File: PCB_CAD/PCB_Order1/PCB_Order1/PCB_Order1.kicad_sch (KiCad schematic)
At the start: 10 parts, among them IC1 TC58BVG1S3HTA00, J1 FW6190, U1 STM32H7A3ZITx, U2 AK5720VT

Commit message: made some small changes to kicad schematic to print
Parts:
- added IC2: AS4C8M16SA-6TCN, SOP80P1176X120-54N, symbol AS4C8M16SA-6TCN:AS4C8M16SA-6TCN
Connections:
- net RAM_A0: now reaches U1.10 (PF0)
- net RAM_A0: now also IC2.23 (A0)
- net RAM_A1: now reaches U1.11 (PF1)
- net RAM_A1: now also IC2.24 (A1)
- net RAM_A2: now reaches U1.12 (PF2)
- net RAM_A2: now also IC2.25 (A2)
- net RAM_A3: now reaches U1.13 (PF3)
- net RAM_A3: now also IC2.26 (A3)
- net RAM_A4: now reaches U1.14 (PF4)
- net RAM_A4: now also IC2.29 (A4)
- net RAM_A5: now reaches U1.15 (PF5)
- net RAM_A5: now also IC2.30 (A5)
- net RAM_A6: now reaches U1.50 (PF12)
- net RAM_A6: now also IC2.31 (A6)
- net RAM_A7: now reaches U1.53 (PF13)
- net RAM_A7: now also IC2.32 (A7)
- net RAM_A8: now reaches U1.54 (PF14)
- net RAM_A8: now also IC2.33 (A8)
- net RAM_A9: now reaches U1.55 (PF15)
- net RAM_A9: now also IC2.34 (A9)
- net RAM_A10: now reaches U1.56 (PG0)
- net RAM_A10: now also IC2.22 (A10/AP)
- net RAM_A11: now reaches U1.57 (PG1)
- net RAM_A11: now also IC2.35 (A11)
- net RAM_BA0: now reaches U1.89 (PG4)
- net RAM_BA0: now also IC2.20 (BA0)
- net RAM_BA1: now reaches U1.90 (PG5)
- net RAM_BA1: now also IC2.21 (BA1)
- new net RAM_ChipEnable: IC2.19 (CS#)
- new net RAM_Clock: IC2.38 (CLK)
- new net RAM_ClockEnable: IC2.37 (CKE)
- new net RAM_ColumnStrobe: IC2.17 (CAS#)
- new net RAM_DQ0: IC2.2 (DQ0)
- new net RAM_DQ1: IC2.4 (DQ1)
- new net RAM_DQ10: IC2.45 (DQ10)
- new net RAM_DQ11: IC2.47 (DQ11)
- new net RAM_DQ12: IC2.48 (DQ12)
- new net RAM_DQ13: IC2.50 (DQ13)
- new net RAM_DQ14: IC2.51 (DQ14)
- new net RAM_DQ15: IC2.53 (DQ15)
- new net RAM_DQ2: IC2.5 (DQ2)
- new net RAM_DQ3: IC2.7 (DQ3)
- new net RAM_DQ4: IC2.8 (DQ4)
- new net RAM_DQ5: IC2.10 (DQ5)
- new net RAM_DQ6: IC2.11 (DQ6)
- new net RAM_DQ7: IC2.13 (DQ7)
- new net RAM_DQ8: IC2.42 (DQ8)
- new net RAM_DQ9: IC2.44 (DQ9)
- new net RAM_LDQM: IC2.15 (LDQM)
- new net RAM_RowStrobe: IC2.18 (RAS#)
- new net RAM_UDQM: IC2.39 (UDQM)
- new net RAM_WriteEnable: IC2.16 (WE#)
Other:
- moved on the sheet: C1, C2, C3, C4, C5, C6, IC1, J1, U1, U2

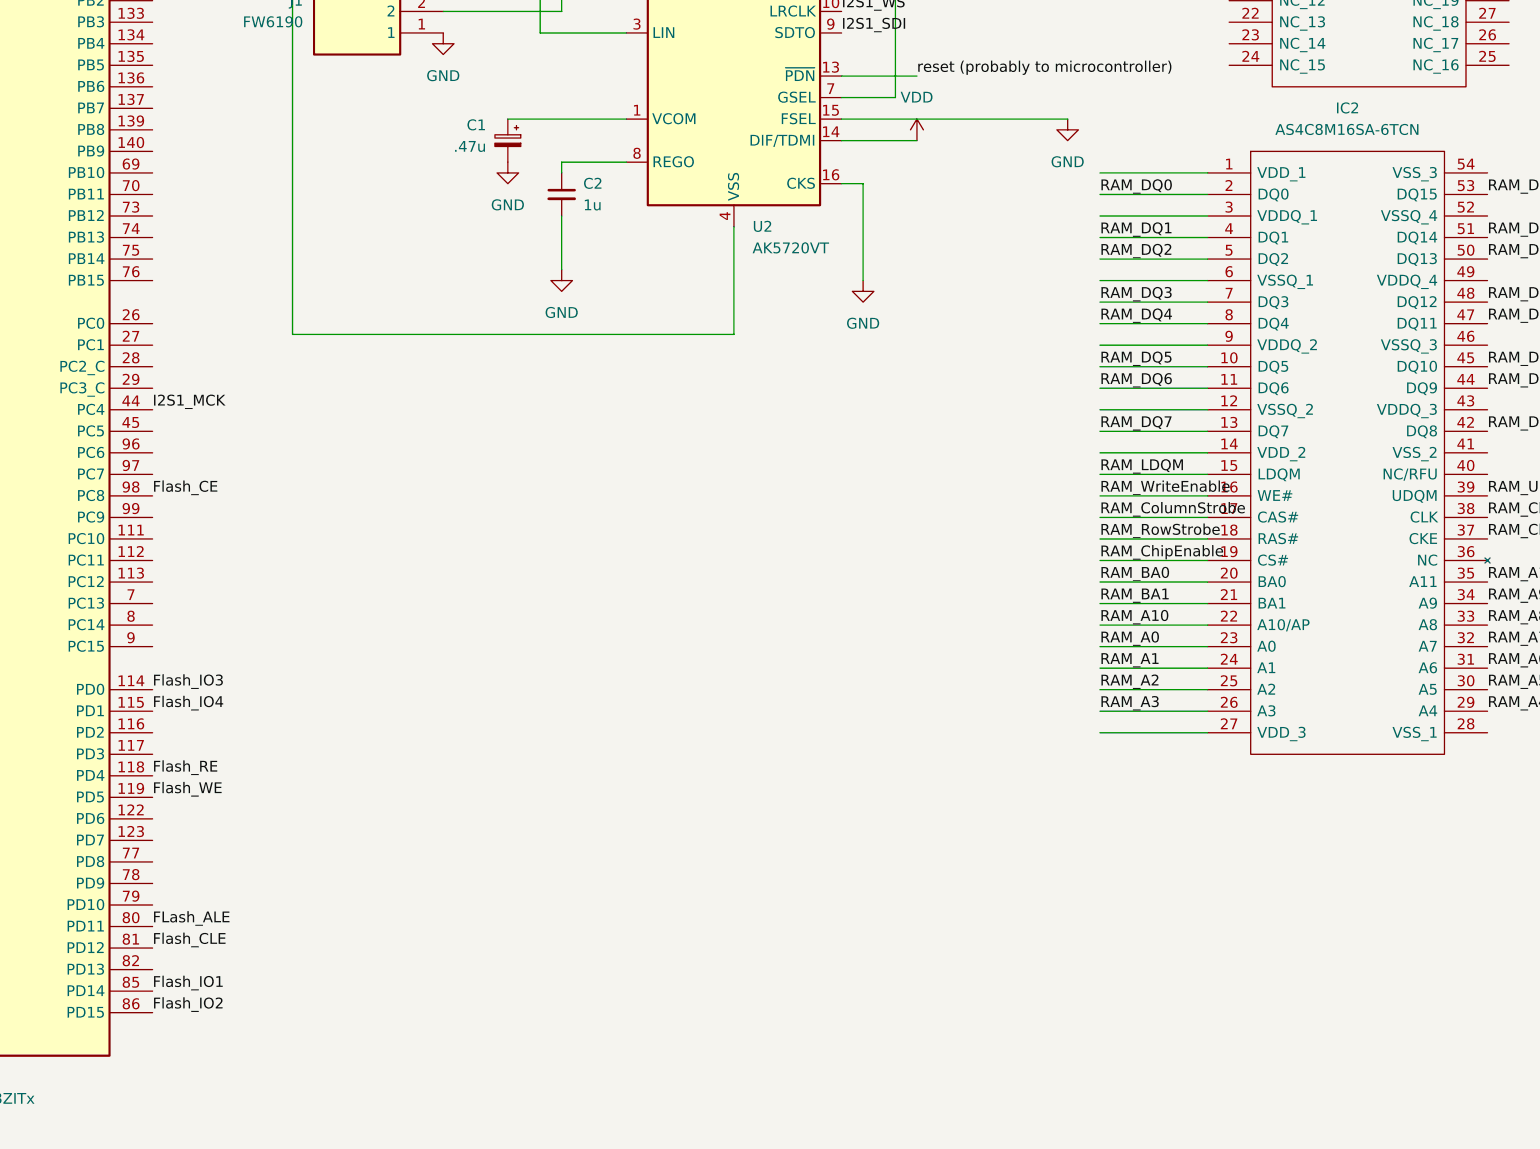
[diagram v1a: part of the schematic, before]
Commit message: schematic add NAU8402WG DAC
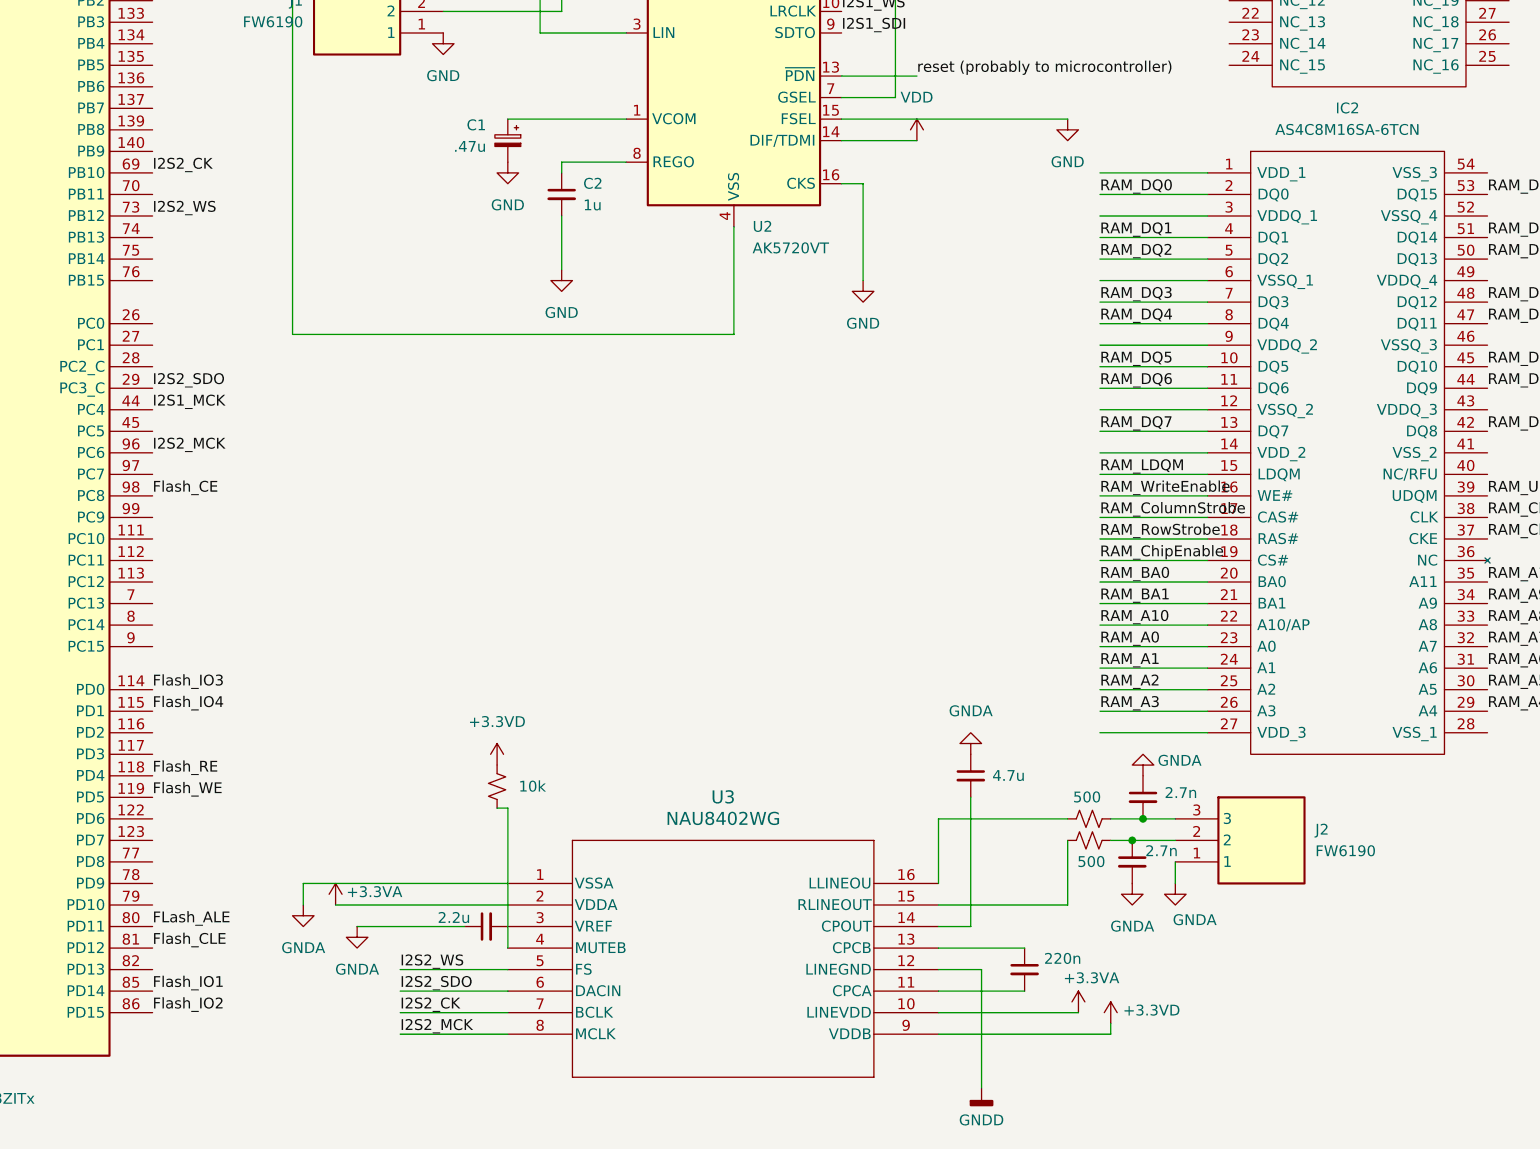
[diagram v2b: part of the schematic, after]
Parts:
- added CPC: 220n, symbol Device:C_Small
- added Chargepump_out: 4.7u, symbol Device:C_Small
- added DacLout_cap, DacRout_cap: 2.7n, symbol Device:C_Small
- added DacLout_res, DacRout_res: 500, symbol Device:R_Small_US
- added Dac_vref: 2.2u, symbol Device:C_Small
- added J2: FW6190, FW6190, symbol FW6190:FW6190
- added Mute_tie: 10k, symbol Device:R_Small_US
- added U3: NAU8402WG, TSSOP16_NAU8402_NUV, symbol NAU8402WG:NAU8402WG
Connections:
- net I2S2_SDO: now reaches U1.29 (PC3_C)
- net I2S2_SDO: now also U3.6 (DACIN)
- net I2S2_CK: now reaches U1.69 (PB10)
- net I2S2_CK: now also U3.7 (BCLK)
- net I2S2_WS: now reaches U1.73 (PB12)
- net I2S2_WS: now also U3.5 (FS)
- net I2S2_MCK: now reaches U1.96 (PC6)
- net I2S2_MCK: now also U3.8 (MCLK)
- new net: DacLout_res.1, U3.16 (LLINEOU)
- new net: DacLout_cap.2, DacLout_res.2, J2.3
- new net: CPC.1, U3.13 (CPCB)
- new net: CPC.2, U3.11 (CPCA)
- new net: DacRout_res.1, U3.15 (RLINEOUT)
- new net: DacRout_cap.1, DacRout_res.2, J2.2
- new net: Chargepump_out.2, U3.14 (CPOUT)
- new net: Dac_vref.2, U3.3 (VREF)
- new net: Mute_tie.2, U3.4 (MUTEB)
- new net +3.3VA: U3.10 (LINEVDD), U3.2 (VDDA)
- new net +3.3VD: Mute_tie.1, U3.9 (VDDB)
- new net GNDA: Chargepump_out.1, DacLout_cap.1, DacRout_cap.2, Dac_vref.1, J2.1, U3.1 (VSSA)
- new net GNDD: U3.12 (LINEGND)

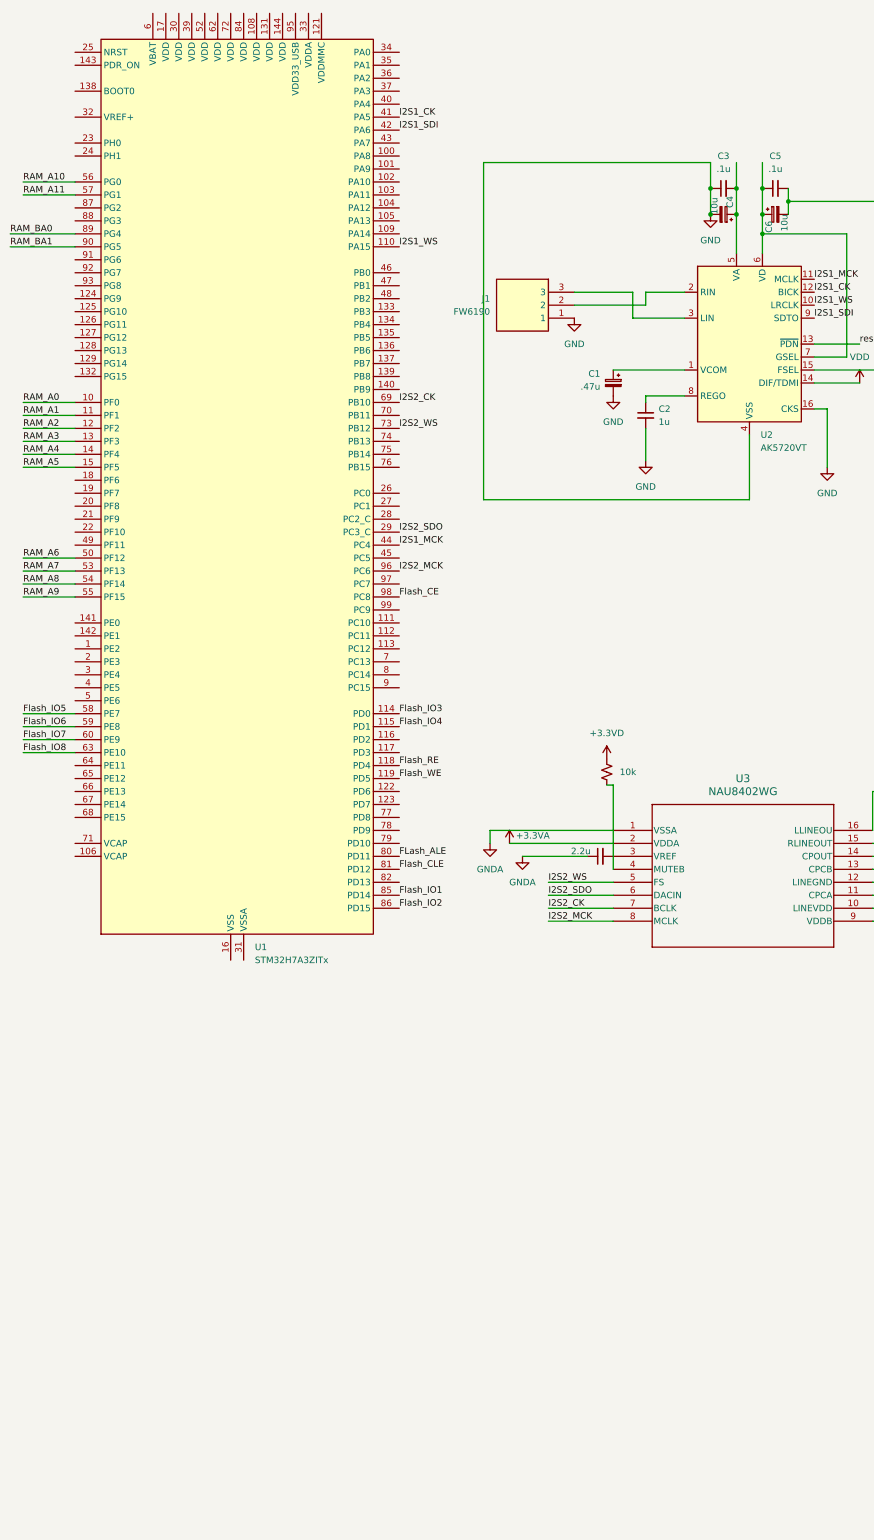
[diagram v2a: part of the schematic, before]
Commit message: add spdif tx output, fixed DIX9211 cad model
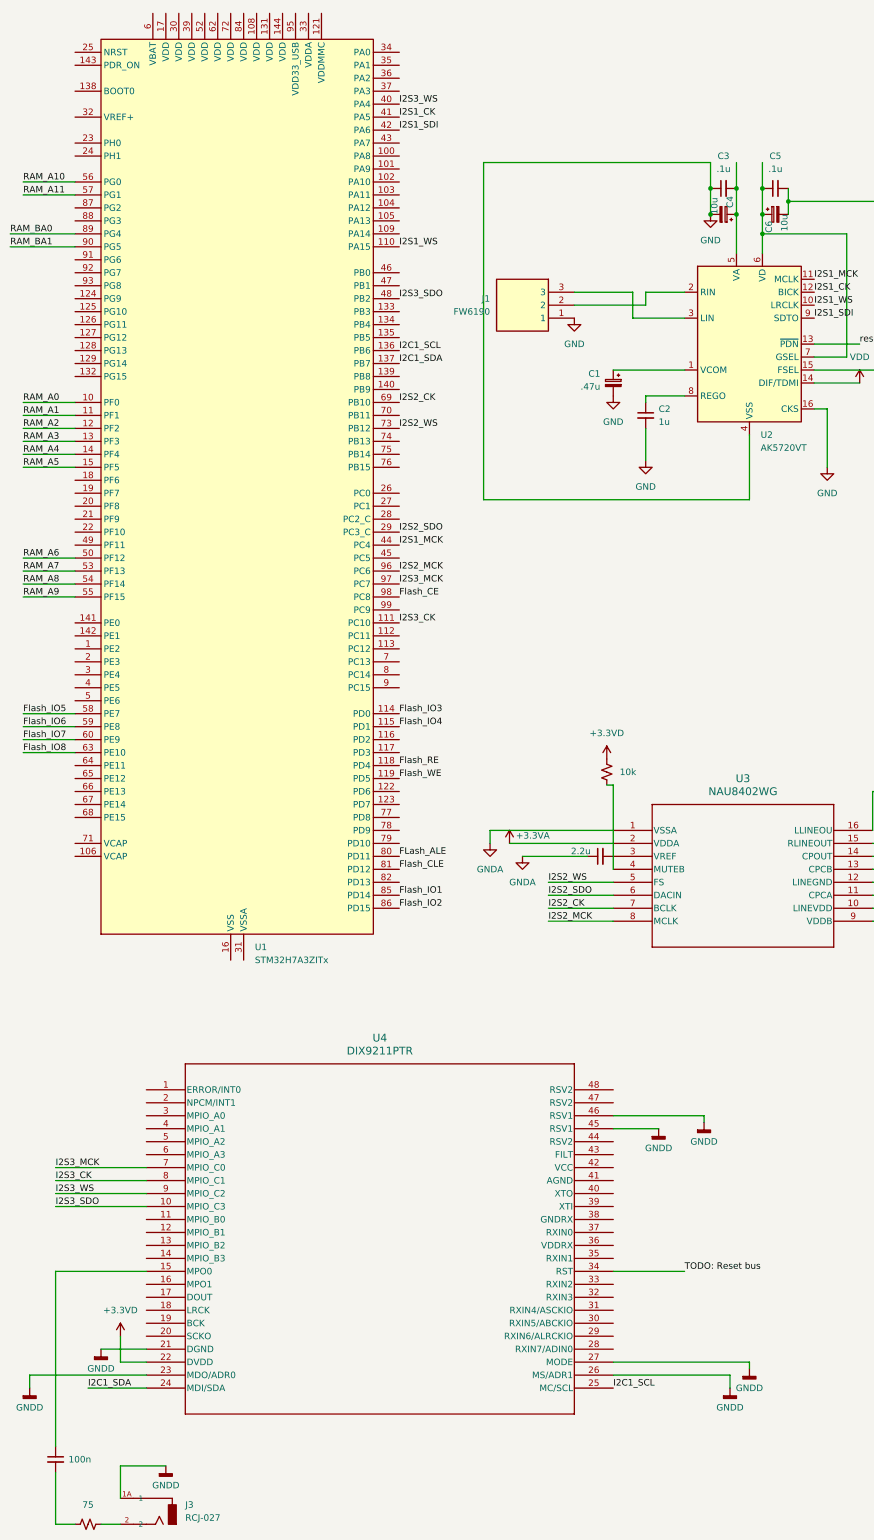
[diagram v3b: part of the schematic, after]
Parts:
- added J3: RCJ-027, RCJ-027:CUI_RCJ-027, symbol RCJ-027:RCJ-027
- added U4: DIX9211PTR, PT48, symbol DIX9211PTR:DIX9211PTR
- added acCoupling_spdif: 100n, symbol Device:C_Small
- added spdif_origination: 75, symbol Device:R_Small_US
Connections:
- net +3.3VD: now also U4.22 (DVDD)
- net GNDD: now also J3.1A (1), U4.21 (DGND), U4.23 (MDO/ADR0), U4.26 (MS/ADR1), U4.27 (MODE), U4.45 (RSV1), U4.46 (RSV1)
- net I2S3_CK: now reaches U1.111 (PC10)
- net I2S3_CK: now also U4.8 (MPIO_C1)
- net I2C1_SCL: now reaches U1.136 (PB6)
- net I2C1_SCL: now also U4.25 (MC/SCL)
- net I2C1_SDA: now reaches U1.137 (PB7)
- net I2C1_SDA: now also U4.24 (MDI/SDA)
- net I2S3_WS: now reaches U1.40 (PA4)
- net I2S3_WS: now also U4.9 (MPIO_C2)
- net I2S3_SDO: now reaches U1.48 (PB2)
- net I2S3_SDO: now also U4.10 (MPIO_C3)
- net I2S3_MCK: now reaches U1.97 (PC7)
- net I2S3_MCK: now also U4.7 (MPIO_C0)
- new net: U4.15 (MPO0), acCoupling_spdif.1
- new net: acCoupling_spdif.2, spdif_origination.1
- new net: J3.2, spdif_origination.2
- new net TODO: Reset bus: U4.34 (RST)
